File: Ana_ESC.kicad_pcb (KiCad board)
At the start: 2 copper layers, 100 x 100 mm, 95 parts, among them IC3 TCAN330DCNT, J1 BM04B-GHS-TBT_LF__SN__N_, J2 Conn_01x04_Pin, J3 USB_C_Receptacle_USB2.0_16P, J4 BM04B-GHS-TBT_LF__SN__N_, J5 Conn_01x02_Socket, Q10 STL90N6F7, Q11 STL90N6F7, Q12 STL90N6F7, Q7 STL90N6F7, Q8 STL90N6F7, Q9 STL90N6F7, SW1 SW_SPDT, SW2 SW_SPDT, U1 DRV8323RSRGZR, U2 STM32G431CBU6, U3 ME6211C33M5, Y1 ECS-80-20-5PX-TR

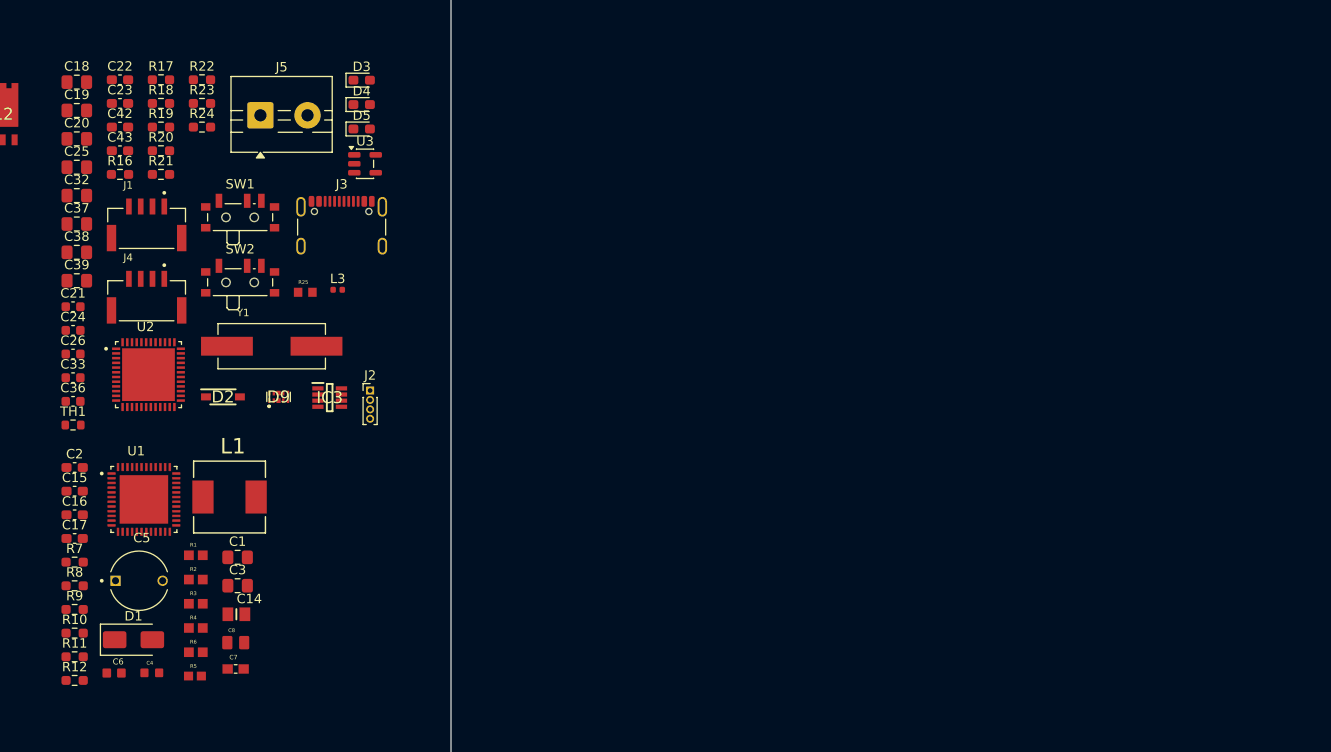
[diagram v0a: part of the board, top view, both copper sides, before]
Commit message: starting with pcb (kicad_pcb 	(version 20241229) 	(generator "pcbnew") 	(generator_version "9.0") 	(layers 		(0 "F.Cu" signal) 		(2 "B.Cu" signal) 		(9 "F.Adhes" user "F.Adhesive") 		(11 "B.Adhes" user "B.Adhesive") 		(13 "F.Paste" user) 		(15 "B.Paste" user) 		(5 "F.SilkS" user "F.Silkscreen") 		(7 "B.SilkS" user "B.Silkscreen") 		(1 "F.Mask" user) 		(3 "B.Mask" user) 		(17 "Dwgs.User" user "User.Drawings") 		(19 "Cmts.User" user "User.Comments") 		(21 "Eco1.User" user "User.Eco1") 		(23 "Eco2.User" user "User.Eco2") 		(25 "Edge.Cuts" user) 		(27 "Margin" user) 		(31 "F.CrtYd" user "F.Courtyard") 		(29 "B.CrtYd" user "B.Courtyard") 		(35 "F.Fab" user) 		(33 "B.Fab" user) 		(39 "User.1" user) 		(41 "User.2" user) 		(43 "User.3" user) 		(45 "User.4" user) 	) 	(net 0 "") 	(net 1 "Net-(U1-CPH)") 	(net 2 "Net-(U1-CPL)") 	(net 3 "/Gate_Driver/DVDD") 	(net 4 "GND") 	(net 5 "/Gate_Driver/AGND") 	(net 6 "Net-(U1-VCP)") 	(net 7 "Net-(D1-K)") 	(net 8 "Net-(U1-CB)") 	(net 9 "MCU_PWR") 	(net 10 "/Gate_Driver/SENS1") 	(net 11 "/Gate_Driver/SENS2") 	(net 12 "/Gate_Driver/SENS3") 	(net 13 "+3.3V") 	(net 14 "/MCU/NTC_FET") 	(net 15 "/MCU/RST") 	(net 16 "+3.3VA") 	(net 17 "/MCU/NTC_MTR") 	(net 18 "/MCU/VBus") 	(net 19 "Net-(D3-A)") 	(net 20 "Net-(D4-A)") 	(net 21 "Net-(D5-A)") 	(net 22 "unconnected-(D9-IO_4-Pad5)") 	(net 23 "/MCU/USB_DP") 	(net 24 "/MCU/USB_DN") 	(net 25 "/MCU/VBUS") 	(net 26 "unconnected-(D9-NC_4-Pad10)") 	(net 27 "/MCU/UART_P") 	(net 28 "/MCU/UART_N") 	(net 29 "Net-(IC3-CANH)") 	(net 30 "/MCU/PD2") 	(net 31 "Net-(IC3-CANL)") 	(net 32 "Net-(IC3-SHDN)") 	(net 33 "unconnected-(J1-Pad1)") 	(net 34 "Net-(C18-Pad1)") 	(net 35 "/MCU/SWDIO") 	(net 36 "/MCU/SWCLK") 	(net 37 "unconnected-(J3-CC2-PadB5)") 	(net 38 "unconnected-(J3-CC1-PadA5)") 	(net 39 "unconnected-(J3-SBU1-PadA8)") 	(net 40 "unconnected-(J3-SBU2-PadB8)") 	(net 41 "/MCU/I2C1_SDA") 	(net 42 "/MCU/I2C1_SCL") 	(net 43 "/Gate_Driver/SHA") 	(net 44 "Net-(Q7-G)") 	(net 45 "/Gate_Driver/SPA") 	(net 46 "Net-(Q8-G)")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
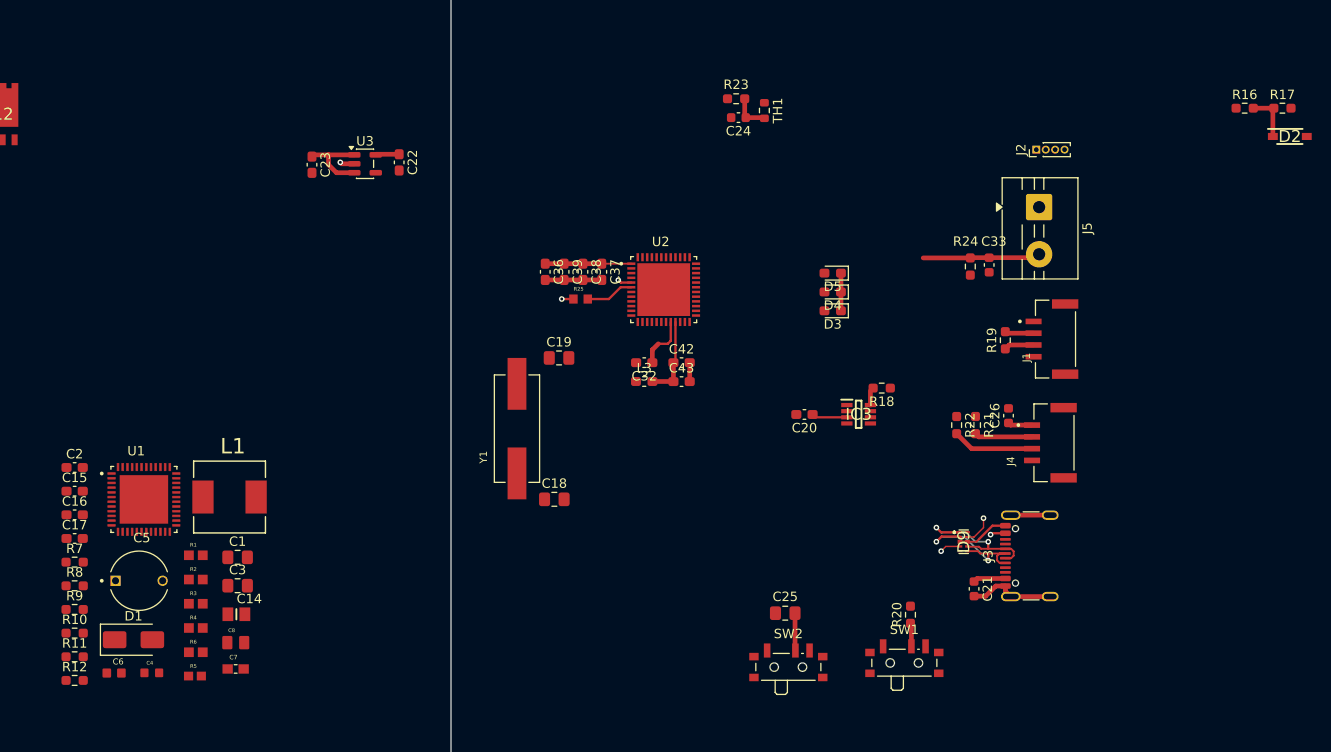
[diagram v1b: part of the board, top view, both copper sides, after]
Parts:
- C20, C32, C37, C38, C39: footprint Capacitor_SMD:C_0805_2012Metric_Pad1.18x1.45mm_HandSolder -> Capacitor_SMD:C_0603_1608Metric_Pad1.08x0.95mm_HandSolder
- C36: footprint Capacitor_SMD:C_0603_1608Metric -> Capacitor_SMD:C_0603_1608Metric_Pad1.08x0.95mm_HandSolder
- L3: footprint Inductor_SMD:L_0402_1005Metric -> Inductor_SMD:L_0603_1608Metric_Pad1.05x0.95mm_HandSolder
- moved R16 119.5 mm to (237.2, 67.5)
- moved R17 119.0 mm to (241.2, 67.5)
- moved D2 116.5 mm to (242.0, 70.5)
- moved C21 100.2 mm to (208.5, 118.5), turned to -90 degrees
- moved C26 99.5 mm to (212.2, 100.1), turned to 90 degrees
- moved J4 98.3 mm to (218.0, 103.0), turned to 90 degrees
- moved J1 98.0 mm to (218.2, 92.0), turned to 90 degrees
- moved C33 97.9 mm to (210.1, 84.1), turned to -90 degrees
- moved R20 93.5 mm to (201.8, 121.2), turned to 90 degrees
- moved R19 92.4 mm to (211.8, 92.1), turned to 90 degrees
- moved R21 90.4 mm to (208.7, 101.1), turned to -90 degrees
- moved C25 88.8 mm to (188.5, 121.1), turned to 180 degrees
- moved R22 88.1 mm to (206.7, 101.1), turned to -90 degrees
- moved SW1 84.9 mm to (201.1, 126.0)
- moved J5 83.2 mm to (215.4, 78.0), turned to -90 degrees
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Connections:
- net PVDD renamed VM
- C14 pad 1: GND -> /Gate_Driver/AGND
- C14 pad 2: MCU_PWR -> +3.3V
- C2 pad 2: GND -> /Gate_Driver/AGND
- C3 pad 1: GND -> /Gate_Driver/BGND
- U1 pad 26: MCU_PWR -> +3.3V
- U1 pad 27: GND -> /Gate_Driver/DGND
- U1 pad 35: GND -> /Gate_Driver/AGND
- U1 pad 43: GND -> /Gate_Driver/BGND
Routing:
- net GND: track 0.00 -> 33.0 mm, vias 0 -> 1
- net +3.3V: track 0.00 -> 18.0 mm
- net /MCU/USB_DN: track 0.00 -> 16.8 mm, vias 0 -> 2
- net /MCU/USB_DP: track 0.00 -> 16.1 mm, vias 0 -> 2
- net +3.3VA: track 0.00 -> 14.4 mm
- net MCU_PWR: track 0.00 -> 13.8 mm, vias 0 -> 1
- net /MCU/NTC_MTR: track 0.00 -> 12.5 mm
- net /MCU/I2C1_SDA: track 0.00 -> 8.66 mm
- net /MCU/I2C1_SCL: track 0.00 -> 6.14 mm
- net /MCU/VBUS: track 0.00 -> 5.32 mm, vias 0 -> 2
- net /MCU/VBus: track 0.00 -> 5.22 mm
- net Net-(U2-PF1-OSC_OUT): track 0.00 -> 5.14 mm
- net /MCU/NTC_FET: track 0.00 -> 4.05 mm
- net /MCU/RST: track 0.00 -> 3.98 mm
- net Net-(IC3-CANL): track 0.00 -> 3.17 mm
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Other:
- copper layers 2 -> 4

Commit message: ja
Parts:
- moved Q8 18.4 mm to (55.0, 61.2), turned to 90 degrees
- moved Q10 18.4 mm to (73.6, 57.3)
- moved R18 13.6 mm to (209.7, 89.2)
- moved C20 13.6 mm to (201.5, 92.0)
- moved IC3 13.6 mm to (207.2, 92.0)
- moved Q11 6.65 mm to (89.9, 68.1)
- moved Q7 6.27 mm to (70.1, 68.1)
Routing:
- net Net-(U2-PF0-OSC_IN): track 1.48 -> 6.05 mm
- net Net-(C18-Pad1): track 1.24 -> 5.30 mm
- added copper zone on F.Cu, net VM
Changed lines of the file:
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@@
 	(footprint "STL90N6F7:STL90N6F7"
 		(layer "F.Cu")
-		(at 63.7916 68.1316)
+		(at 70.062 68.125)
 		(descr "PowerFLAt5x6_23")
 		(tags "MOSFET (N-Channel)")
@@
 	(footprint "LIB_TCAN330DCNT:SOT65P280X145-8N"
 		(layer "F.Cu")
-		(at 196.25 99.975)
+		(at 207.25 92)
 		(descr "DCN (R-PDSO-G8)_2021")
 		(tags "Integrated Circuit")
@@
 	(footprint "STL90N6F7:STL90N6F7"
 		(layer "F.Cu")
-		(at 88.3916 68.1316)
+		(at 73.595 57.275)
 		(descr "PowerFLAt5x6_23")
 		(tags "MOSFET (N-Channel)")
@@
 	(footprint "Capacitor_SMD:C_0603_1608Metric_Pad1.08x0.95mm_HandSolder"
 		(layer "F.Cu")
-		(at 190.5 100 180)
+		(at 201.5 92.025 180)
 		(descr "Capacitor SMD 0603 (1608 Metric), square (rectangular) end terminal, IPC-7351 nominal with elongated pad for handsoldering. (Body size source: IPC-SM-782 page 76, https://www.pcb-3d.com/wordpress/wp-content/uploads/ipc-sm-782a_amendment_1_and_2.pdf), generated with kicad-footprint-generator")
 		(tags "capacitor handsolder")
@@
 	(footprint "STL90N6F7:STL90N6F7"
 		(layer "F.Cu")
-		(at 71.9916 68.1316)
+		(at 54.975 61.205 90)
 		(descr "PowerFLAt5x6_23")
 		(tags "MOSFET (N-Channel)")
 		(property "Reference" "Q8"
-			(at 0 0 0)
+			(at 0 0 90)
 			(layer "F.SilkS")
 			(effects
@@
 		)
 		(property "Value" "STL90N6F7"
-			(at 0 0 0)
+			(at 0 0 90)
 			(layer "F.SilkS")
 			(hide yes)
@@
 		)
 		(property "Datasheet" "https://www.st.com/resource/en/datasheet/stl90n6f7.pdf"
-			(at 0 0 0)
+			(at 0 0 90)
 			(layer "F.Fab")
 			(hide yes)
@@
 		)
 		(property "Description" "N-channel 60 V, 4.6 m typ., 90 A STripFET F7 Power MOSFET in a PowerFLAT 5x6 package"
-			(at 0 0 0)
+			(at 0 0 90)
 			(layer "F.Fab")
 			(hide yes)
@@
 		)
 		(property "Height" "1"
-			(at 0 0 0)
+			(at 0 0 90)
 			(unlocked yes)
 			(layer "F.Fab")
@@
 		)
 		(property "Manufacturer_Name" "STMicroelectronics"
-			(at 0 0 0)
+			(at 0 0 90)
 			(unlocked yes)
 			(layer "F.Fab")
@@
 		)
 		(property "Manufacturer_Part_Number" "STL90N6F7"
-			(at 0 0 0)
+			(at 0 0 90)
 			(unlocked yes)
 			(layer "F.Fab")
@@
 		)
 		(property "Mouser Part Number" "511-STL90N6F7"
-			(at 0 0 0)
+			(at 0 0 90)
 			(unlocked yes)
 			(layer "F.Fab")
@@
 		)
 		(property "Mouser Price/Stock" "https://www.mouser.co.uk/ProductDetail/STMicroelectronics/STL90N6F7?qs=bKenfurwlsmCpdlaRCdwag%3D%3D"
-			(at 0 0 0)
+			(at 0 0 90)
 			(unlocked yes)
 			(layer "F.Fab")
@@
 		)
 		(property "Arrow Part Number" "STL90N6F7"
-			(at 0 0 0)
+			(at 0 0 90)
 			(unlocked yes)
 			(layer "F.Fab")
@@
 		)
 		(property "Arrow Price/Stock" "https://www.arrow.com/en/products/stl90n6f7/stmicroelectronics?region=nac"
-			(at 0 0 0)
+			(at 0 0 90)
 			(unlocked yes)
 			(layer "F.Fab")
@@
 		)
 		(fp_line
-			(start -3.55 -4.35)
-			(end 3.55 -4.35)
+			(start 3.55 -4.35)
+			(end 3.55 4.35)
 			(stroke
 				(width 0.1)
@@
 		)
 		(fp_line
-			(start -3.55 4.35)
-			(end -3.55 -4.35)
+			(start -3.55 -4.35)
+			(end 3.55 -4.35)
 			(stroke
 				(width 0.1)
@@
 		)
 		(fp_line
-			(start 3.55 -4.35)
-			(end 3.55 4.35)
+			(start 3.55 4.35)
+			(end -3.55 4.35)
 			(stroke
 				(width 0.1)
@@
 		)
 		(fp_line
-			(start 3.55 4.35)
-			(end -3.55 4.35)
+			(start -3.55 4.35)
+			(end -3.55 -4.35)
 			(stroke
 				(width 0.1)
@@
 		)
 		(fp_line
-			(start -2.55 -3.063)
-			(end 2.55 -3.063)
+			(start 2.55 -3.063)
+			(end 2.55 3.063)
 			(stroke
 				(width 0.1)
@@
 		)
 		(fp_line
-			(start -2.55 3.063)
-			(end -2.55 -3.063)
+			(start -2.55 -3.063)
+			(end 2.55 -3.063)
 			(stroke
 				(width 0.1)
@@
 		)
 		(fp_line
-			(start 2.55 -3.063)
-			(end 2.55 3.063)
+			(start 2.55 3.063)
+			(end -2.55 3.063)
 			(stroke
 				(width 0.1)
@@
 		)
 		(fp_line
-			(start 2.55 3.063)
-			(end -2.55 3.063)
+			(start -2.55 3.063)
+			(end -2.55 -3.063)
 			(stroke
 				(width 0.1)
@@
 		)
 		(fp_text user "${REFERENCE}"
-			(at 0 0 0)
+			(at 0 0 90)
 			(layer "F.Fab")
 			(effects
@@
 		)
 		(pad "1" smd rect
-			(at -1.905 2.725)
+			(at -1.905 2.725 90)
 			(size 0.65 1.15)
 			(layers "F.Cu" "F.Mask" "F.Paste")
@@
 		)
 		(pad "2" smd rect
-			(at -0.635 2.725)
+			(at -0.635 2.725 90)
 			(size 0.65 1.15)
 			(layers "F.Cu" "F.Mask" "F.Paste")
@@
 		)
 		(pad "3" smd rect
-			(at 0.635 2.725)
+			(at 0.635 2.725 90)
 			(size 0.65 1.15)
 			(layers "F.Cu" "F.Mask" "F.Paste")
@@
 		)
 		(pad "4" smd rect
-			(at 1.905 2.725)
+			(at 1.905 2.725 90)
 			(size 0.65 1.15)
 			(layers "F.Cu" "F.Mask" "F.Paste")
@@
 		)
 		(pad "5" smd rect
-			(at 1.938 -3.025 90)
+			(at 1.938 -3.025 180)
 			(size 0.55 0.725)
 			(layers "F.Cu" "F.Mask" "F.Paste")
@@
 		)
 		(pad "6" smd rect
-			(at 0.675 -3.025 90)
+			(at 0.675 -3.025 180)
 			(size 0.55 0.725)
 			(layers "F.Cu" "F.Mask" "F.Paste")
@@
 		)
 		(pad "7" smd rect
-			(at -0.675 -3.025 90)
+			(at -0.675 -3.025 180)
 			(size 0.55 0.725)
 			(layers "F.Cu" "F.Mask" "F.Paste")
@@
 		)
 		(pad "8" smd rect
-			(at -1.938 -3.025 90)
+			(at -1.938 -3.025 180)
 			(size 0.55 0.725)
 			(layers "F.Cu" "F.Mask" "F.Paste")
@@
 		)
 		(pad "9" smd rect
-			(at 0 -0.7 90)
+			(at 0 -0.7 180)
 			(size 4.1 4.6)
 			(layers "F.Cu" "F.Mask" "F.Paste")
@@
 	(footprint "Resistor_SMD:R_0603_1608Metric_Pad0.98x0.95mm_HandSolder"
 		(layer "F.Cu")
-		(at 198.7 97.2 180)
+		(at 209.7 89.225 180)
 		(descr "Resistor SMD 0603 (1608 Metric), square (rectangular) end terminal, IPC-7351 nominal with elongated pad for handsoldering. (Body size source: IPC-SM-782 page 72, https://www.pcb-3d.com/wordpress/wp-content/uploads/ipc-sm-782a_amendment_1_and_2.pdf), generated with kicad-footprint-generator")
 		(tags "resistor handsolder")
@@
 	(footprint "STL90N6F7:STL90N6F7"
 		(layer "F.Cu")
-		(at 96.5916 68.1316)
+		(at 89.938 68.1316)
 		(descr "PowerFLAt5x6_23")
 		(tags "MOSFET (N-Channel)")
@@
 	)
 	(segment
-		(start 191.6625 100.3)
-		(end 191.3625 100)
+		(start 202.6625 92.325)
+		(end 202.3625 92.025)
 		(width 0.25)
 		(layer "F.Cu")
@@
 	)
 	(segment
-		(start 195 100.3)
-		(end 191.6625 100.3)
+		(start 206 92.325)
+		(end 202.6625 92.325)
 		(width 0.25)
 		(layer "F.Cu")
@@
 	)
 	(segment
-		(start 197.5 97.4875)
-		(end 197.7875 97.2)
+		(start 208.5 89.5125)
+		(end 208.7875 89.225)
 		(width 0.2)
 		(layer "F.Cu")
@@
 	)
 	(segment
-		(start 197.5 99)
-		(end 197.5 97.4875)
+		(start 208.5 91.025)
+		(end 208.5 89.5125)
 		(width 0.5)
 		(layer "F.Cu")
@@
 	)
 	(segment
+		(start 162.75 109)
+		(end 160 106.25)
+		(width 0.5)
+		(layer "F.Cu")
+		(net 34)
+	)
+	(segment
 		(start 165.99 87.75)
 		(end 164.75 87.75)
@@
 		(net 34)
 	)
+	(segment
+		(start 162.925 109)
+		(end 162.75 109)
+		(width 0.5)
+		(layer "F.Cu")
+		(net 34)
+	)
 	(via
 		(at 164.75 87.75)
@@
 	)
 	(segment
+		(start 163.425 94)
+		(end 162.75 94)
+		(width 0.5)
+		(layer "F.Cu")
+		(net 93)
+	)
+	(segment
 		(start 171 86)
 		(end 170.75 85.75)
@@
 		(net 93)
 	)
+	(segment
+		(start 162.75 94)
+		(end 160 96.75)
+		(width 0.5)
+		(layer "F.Cu")
+		(net 93)
+	)
 	(via
 		(at 170.75 85.75)
@@
 	)
 	(zone
+		(net 99)
+		(net_name "VM")
+		(layer "F.Cu")
+		(hatch edge 0.5)
+		(connect_pads
+			(clearance 0.5)
+		)
+		(min_thickness 0.25)
+		(filled_areas_thickness no)
+		(fill yes
+			(thermal_gap 0.5)
+			(thermal_bridge_width 0.5)
+		)
+		(polygon
+			(pts
+				(xy 93.5 63.5) (xy 93.5 69.5) (xy 66.5 69.5) (xy 66.5 63.5)
+			)
+		)
+	)
+	(zone

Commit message: d;akljadsl;kdsj
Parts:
- C7: footprint CC0603KRX7R7BB104:CAPC1608X90 -> Capacitor_SMD:C_0603_1608Metric_Pad1.08x0.95mm_HandSolder
- C8: footprint CL21A226KOQNNNE:CAPC2012X140N -> Capacitor_SMD:C_0805_2012Metric_Pad1.18x1.45mm_HandSolder
- moved D2 155.2 mm to (96.3, 124.0)
- moved R16 155.2 mm to (91.5, 121.0)
- moved R17 155.2 mm to (95.5, 121.0)
- moved C8 55.2 mm to (131.0, 69.0), turned to 90 degrees
- moved R4 55.2 mm to (126.8, 67.5)
- moved R5 55.2 mm to (126.7, 72.6)
- moved D1 51.4 mm to (118.5, 72.5), turned to 180 degrees
- moved C7 49.3 mm to (121.5, 78.5)
- moved C6 45.9 mm to (109.0, 82.2)
- moved L1 43.7 mm to (120.5, 66.0), turned to 90 degrees
- moved R6 42.3 mm to (128.8, 83.0)
- moved C1 34.8 mm to (112.5, 85.2), turned to -90 degrees
- moved C4 34.6 mm to (101.5, 99.0)
- moved C5 30.0 mm to (101.5, 94.0)
- moved R2 28.7 mm to (129.0, 89.0)
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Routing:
- net GND: track 33.0 -> 40.7 mm
- net Net-(U1-CPH): track 0.00 -> 6.96 mm
- net VM: track 0.00 -> 6.67 mm
- net Net-(U1-CPL): track 0.00 -> 6.08 mm
- net Net-(U1-CB): track 0.00 -> 4.73 mm
- net Net-(D1-K): track 0.00 -> 4.23 mm
- net /Gate_Driver/SENS3: track 0.00 -> 4.02 mm
- net /Gate_Driver/SENS1: track 0.00 -> 4.02 mm
- net /Gate_Driver/SENS2: track 0.00 -> 4.00 mm
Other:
- board size 100 x 100 mm -> 180.5 x 100 mm

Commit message: started to pcb design, mosfets,shunts drv8323 placement.
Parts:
- Rsense_A5: footprint CSNL2512FT3L00:RESC6331X75N -> CRF2512-FZ-R002ELF:RESC6432X80N
- moved C33 176.7 mm to (310.3, -61.4)
- moved J1 176.7 mm to (318.3, -53.5)
- moved J2 176.7 mm to (315.3, -73.6)
- moved R24 176.7 mm to (308.3, -61.2)
- moved SW1 176.7 mm to (301.3, -19.5)
- moved SW2 176.7 mm to (289.0, -19.0)
- moved C15 176.7 mm to (211.3, -11.5)
- moved C16 176.7 mm to (218.9, -11.8)
- moved C17 176.7 mm to (225.7, -13.8)
- moved C18 176.7 mm to (264.1, -36.5)
- moved C19 176.7 mm to (264.6, -51.5)
- moved C20 176.7 mm to (301.7, -53.5)
- moved C21 176.7 mm to (308.7, -27.0)
- moved C24 176.7 mm to (283.7, -77.0)
- moved C25 176.7 mm to (288.6, -24.4)
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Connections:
- net /Gate_Driver/SPA renamed /Mosfetv2/A+
- C14 pad 1: /Gate_Driver/AGND -> /Gate_Driver/DGND
- Rsense_A4 pad 1: GND1 -> /Mosfetv2/A-
- Rsense_A5 pad 1: GND1 -> /Mosfetv2/A-
- Rsense_B4 pad 1: GND1 -> GND
- Rsense_B5 pad 1: GND1 -> GND
- Rsense_C4 pad 1: GND1 -> GND
- Rsense_C5 pad 1: GND1 -> GND
- U1 pad 12: GND1 -> /Mosfetv2/A-
- U1 pad 13: GND1 -> GND
- U1 pad 22: GND1 -> GND
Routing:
- net /Gate_Driver/SHA: track 0.00 -> 42.4 mm
- net /Gate_Driver/SHC: track 0.00 -> 34.9 mm
- net /Gate_Driver/SHB: track 0.00 -> 27.2 mm
- net Net-(Q7-G): track 0.00 -> 26.4 mm
- net Net-(Q9-G): track 0.00 -> 23.9 mm
- net Net-(Q11-G): track 0.00 -> 21.4 mm
- net /Gate_Driver/GLA: track 0.00 -> 19.9 mm
- net /Gate_Driver/GHA: track 0.00 -> 19.5 mm
- net Net-(Q12-G): track 0.00 -> 17.5 mm
- net /Gate_Driver/GHC: track 0.00 -> 17.3 mm
- net Net-(U1-FB): track 0.00 -> 16.7 mm
- net Net-(Q10-G): track 0.00 -> 15.3 mm
- net /Gate_Driver/GLC: track 0.00 -> 14.9 mm
- net Net-(Q8-G): track 0.00 -> 14.8 mm
- net /Gate_Driver/FAULT: track 0.00 -> 13.1 mm
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- added copper zone on F.Cu, net /Gate_Driver/DVDD
- added copper zone on F.Cu, net /Gate_Driver/SHA
- added copper zone on F.Cu, net /Gate_Driver/SHB
- added copper zone on F.Cu, net /Gate_Driver/SHC
- added copper zone on F.Cu, net /Gate_Driver/SPB
- added copper zone on F.Cu, net /Gate_Driver/SPC
- added copper zone on F.Cu, net /Mosfetv2/A+
- added copper zone on F.Cu, net GND
- added copper zone on F.Cu, net Net-(D1-K)
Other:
- board size 180.5 x 100 mm -> 100 x 145.5 mm

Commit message: new pcb
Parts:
- added H1: MountingHole, MountingHole:MountingHole_3.2mm_M3, F.Cu at (62.5, 60.2)
- added H2: MountingHole, MountingHole:MountingHole_3.2mm_M3, F.Cu at (122.5, 60.2)
- added H3: MountingHole, MountingHole:MountingHole_3.2mm_M3, F.Cu at (122.5, 120.2)
- added H4: MountingHole, MountingHole:MountingHole_3.2mm_M3, F.Cu at (62.5, 120.2)
- C27, C28, C30: footprint Capacitor_SMD:C_0805_2012Metric_Pad1.18x1.45mm_HandSolder -> Capacitor_SMD:C_1206_3216Metric_Pad1.33x1.80mm_HandSolder
- moved J5 310.3 mm to (71.0, 123.5), turned to 0 degrees
- moved J2 306.1 mm to (57.5, 91.5), turned to 0 degrees
- moved J1 294.9 mm to (84.9, 126.6), turned to 0 degrees
- moved C33 294.6 mm to (75.0, 115.9), turned to 180 degrees
- moved R24 293.9 mm to (75.3, 118.0), turned to 180 degrees
- moved D5 289.1 mm to (78.5, 104.5), turned to 0 degrees
- moved D3 289.1 mm to (78.5, 99.3), turned to 0 degrees
- moved D4 289.1 mm to (78.5, 101.9), turned to 0 degrees
- moved R19 282.4 mm to (88.2, 118.9), turned to 0 degrees
- moved J3 281.0 mm to (58.6, 83.0), turned to -90 degrees
- moved R18 281.0 mm to (88.2, 116.4), turned to 0 degrees
- moved IC3 280.9 mm to (84.0, 116.8), turned to -90 degrees
- moved J4 280.7 mm to (94.1, 126.6), turned to 0 degrees
- moved C20 278.4 mm to (84.3, 120.4), turned to 0 degrees
- moved R20 277.5 mm to (61.2, 113.8), turned to -90 degrees
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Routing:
- net GND: track 40.7 -> 94.2 mm, vias 1 -> 24
- net VM: track 15.0 -> 59.4 mm
- net /Gate_Driver/SPC: track 0.00 -> 26.6 mm, vias 0 -> 2
- net /Mosfetv2/A-: track 0.42 -> 24.9 mm, vias 0 -> 2
- net +3.3V: track 25.9 -> 5.15 mm
- net MCU_PWR: track 20.7 -> 1.36 mm
- net /Mosfetv2/A+: track 0.60 -> 19.8 mm, vias 0 -> 2
- net /Gate_Driver/SPB: track 0.00 -> 15.4 mm, vias 0 -> 2
- net +3.3VA: track 14.4 -> 0.00 mm
- net /MCU/USB_DN: track 16.8 -> 3.27 mm, vias 2 -> 0
- net /MCU/USB_DP: track 16.1 -> 3.27 mm, vias 2 -> 0
- net Net-(U1-FB): track 16.7 -> 6.54 mm
- net /MCU/I2C1_SDA: track 8.66 -> 0.00 mm
- net /Gate_Driver/SHA: track 42.4 -> 35.8 mm
- net Net-(U1-SHDN_N): track 4.03 -> 10.5 mm, vias 0 -> 2
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- added copper zone on B.Cu, net /Gate_Driver/SHA
- added copper zone on In1.Cu, net /Gate_Driver/SHA
- added copper zone on In2.Cu, net /Gate_Driver/SHA
- added copper zone on B.Cu, net /Gate_Driver/SHB
- added copper zone on In1.Cu, net /Gate_Driver/SHB
- added copper zone on In2.Cu, net /Gate_Driver/SHB
- added copper zone on B.Cu, net /Gate_Driver/SHC
- added copper zone on In1.Cu, net /Gate_Driver/SHC
- added copper zone on In2.Cu, net /Gate_Driver/SHC
- added copper zone on B.Cu, net VM
- added copper zone on In1.Cu, net VM
- added copper zone on In2.Cu, net VM
- removed copper zone on F.Cu, net /Gate_Driver/DVDD
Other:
- board size 100 x 145.5 mm -> 75 x 75 mm
